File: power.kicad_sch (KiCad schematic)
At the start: 12 parts, among them J301 USB_C_Receptacle_USB2.0, U301 FTZU6.2ET148, U302 XC9265A331MR-G

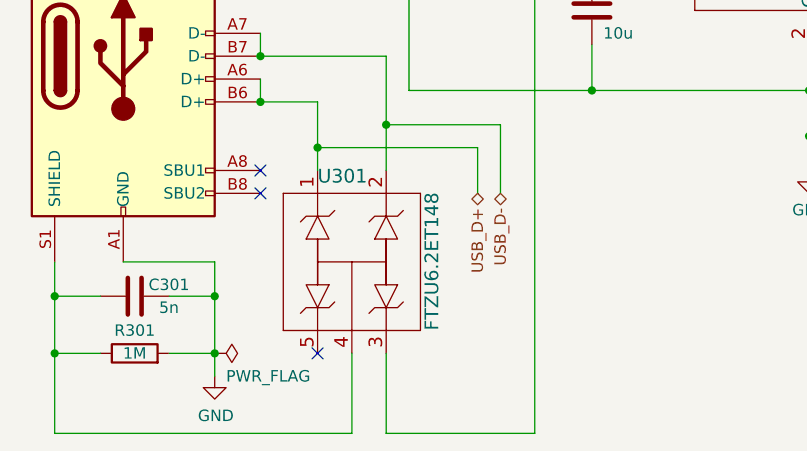
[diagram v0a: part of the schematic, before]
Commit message: replace out of stock components
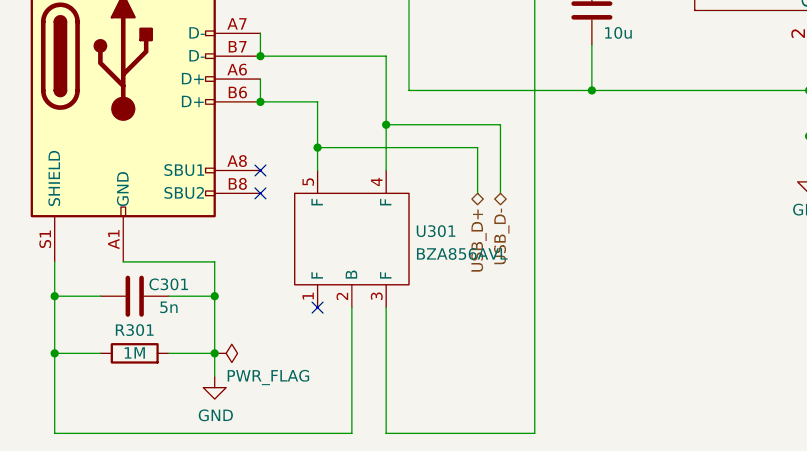
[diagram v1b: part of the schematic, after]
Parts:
- removed U301: FTZU6.2ET148, FTZU6.2ET148:FTZU6.2ET148, symbol FTZU6.2ET148:FTZU6.2ET148
- added U301: BZA856AVL, BZA856AVL:BZA856AVL, symbol BZA956A:BZA956A
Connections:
- net +5V: now also U301.3 (F)
- net USB_D+: now also U301.5 (F)
- net USB_D-: now also U301.4 (F)
- net at C301.1, J301.S1 (SHIELD), R301.1: now also U301.2 (B)
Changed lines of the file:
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@@
   (junction (at 63.5 107.95) (diameter 0) (color 0 0 0 0)
   )
-  (no_connect (at 92.71 114.3))
+  (no_connect (at 92.71 109.22))
   (no_connect (at 86.36 93.98))
   (no_connect (at 86.36 96.52))
@@
     (stroke (width 0) (type default) (color 0 0 0 0))
   )
+  (wire (pts (xy 100.33 109.22) (xy 100.33 123.19))
+    (stroke (width 0) (type default) (color 0 0 0 0))
+  )
   (wire (pts (xy 68.58 114.3) (xy 63.5 114.3))
     (stroke (width 0) (type default) (color 0 0 0 0))
@@
     (stroke (width 0) (type default) (color 0 0 0 0))
   )
-  (wire (pts (xy 96.52 114.3) (xy 96.52 123.19))
-    (stroke (width 0) (type default) (color 0 0 0 0))
-  )
-  (wire (pts (xy 100.33 114.3) (xy 100.33 123.19))
+  (wire (pts (xy 96.52 109.22) (xy 96.52 123.19))
     (stroke (width 0) (type default) (color 0 0 0 0))
   )
@@
   (symbol (lib_id "power:PWR_FLAG") (at 81.28 114.3 270) (unit 1)
     (in_bom yes) (on_board yes)
-    (property "Reference" "#FLG0101" (id 0) (at 83.185 114.3 0)
+    (property "Reference" "#FLG0301" (id 0) (at 83.185 114.3 0)
       (effects (font (size 1.27 1.27)) hide)
     )
@@
   (symbol (lib_id "power:+3V3") (at 181.61 63.5 0) (unit 1)
     (in_bom yes) (on_board yes)
-    (property "Reference" "#PWR0303" (id 0) (at 181.61 67.31 0)
+    (property "Reference" "#PWR0304" (id 0) (at 181.61 67.31 0)
       (effects (font (size 1.27 1.27)) hide)
     )
@@
     (pin "2")
   )
+  (symbol (lib_id "BZA956A:BZA956A") (at 96.52 101.6 0) (unit 1)
+    (in_bom yes) (on_board yes)
+    (property "Reference" "U301" (id 0) (at 103.5812 100.7653 0)
+      (effects (font (size 1.27 1.27)) (justify left))
+    )
+    (property "Value" "BZA856AVL" (id 1) (at 103.5812 103.3022 0)
+      (effects (font (size 1.27 1.27)) (justify left))
+    )
+    (property "Footprint" "BZA856AVL:BZA856AVL" (id 2) (at 96.52 101.6 0)
+      (effects (font (size 1.27 1.27)) hide)
+    )
+    (property "Datasheet" "https://assets.nexperia.com/documents/data-sheet/BZA800AVL_SERIES.pdf" (id 3) (at 96.52 101.6 0)
+      (effects (font (size 1.27 1.27)) hide)
+    )
+    (property "DK" "https://www.digikey.no/no/products/detail/nexperia-usa-inc/BZA856AVL-115/1155404" (id 4) (at 96.52 101.6 0)
+      (effects (font (size 1.27 1.27)) hide)
+    )
+    (pin "1")
+    (pin "2")
+    (pin "3")
+    (pin "4")
+    (pin "5")
+  )
   (symbol (lib_id "Device:R") (at 72.39 114.3 90) (unit 1)
     (in_bom yes) (on_board yes)
@@
     (pin "2")
   )
-  (symbol (lib_id "FTZU6.2ET148:FTZU6.2ET148") (at 96.52 104.14 0) (unit 1)
-    (in_bom yes) (on_board yes)
-    (property "Reference" "U301" (id 0) (at 92.71 94.615 0)
-      (effects (font (size 1.524 1.524)) (justify left))
-    )
-    (property "Value" "FTZU6.2ET148" (id 1) (at 105.41 111.76 90)
-      (effects (font (size 1.524 1.524)) (justify left))
-    )
-    (property "Footprint" "FTZU6.2ET148:FTZU6.2ET148" (id 2) (at 116.205 106.68 0)
-      (effects (font (size 1.524 1.524)) hide)
-    )
-    (property "Datasheet" "" (id 3) (at 96.52 104.14 0)
-      (effects (font (size 1.524 1.524)))
-    )
-    (property "DK" "https://www.digikey.no/no/products/detail/rohm-semiconductor/FTZU6-2ET148/926206" (id 4) (at 96.52 104.14 0)
-      (effects (font (size 1.27 1.27)) hide)
-    )
-    (pin "1")
-    (pin "2")
-    (pin "3")
-    (pin "4")
-    (pin "5")
-  )
   (symbol (lib_id "power:+5V") (at 102.87 63.5 0) (unit 1)
     (in_bom yes) (on_board yes) (fields_autoplaced)
-    (property "Reference" "#PWR0115" (id 0) (at 102.87 67.31 0)
+    (property "Reference" "#PWR0302" (id 0) (at 102.87 67.31 0)
       (effects (font (size 1.27 1.27)) hide)
     )
@@
   (symbol (lib_id "power:GND") (at 147.32 93.98 0) (unit 1)
     (in_bom yes) (on_board yes)
-    (property "Reference" "#PWR0302" (id 0) (at 147.32 100.33 0)
+    (property "Reference" "#PWR0303" (id 0) (at 147.32 100.33 0)
       (effects (font (size 1.27 1.27)) hide)
     )
@@
   (symbol (lib_id "power:PWR_FLAG") (at 93.98 63.5 0) (unit 1)
     (in_bom yes) (on_board yes) (fields_autoplaced)
-    (property "Reference" "#FLG0103" (id 0) (at 93.98 61.595 0)
-      (effects (font (size 1.27 1.27)) hide)
-    )
+    (property "Reference" "#FLG0302" (id 0) (at 93.98 61.595 0)
+      (effects (font (size 1.27 1.27)) hide)
+    )

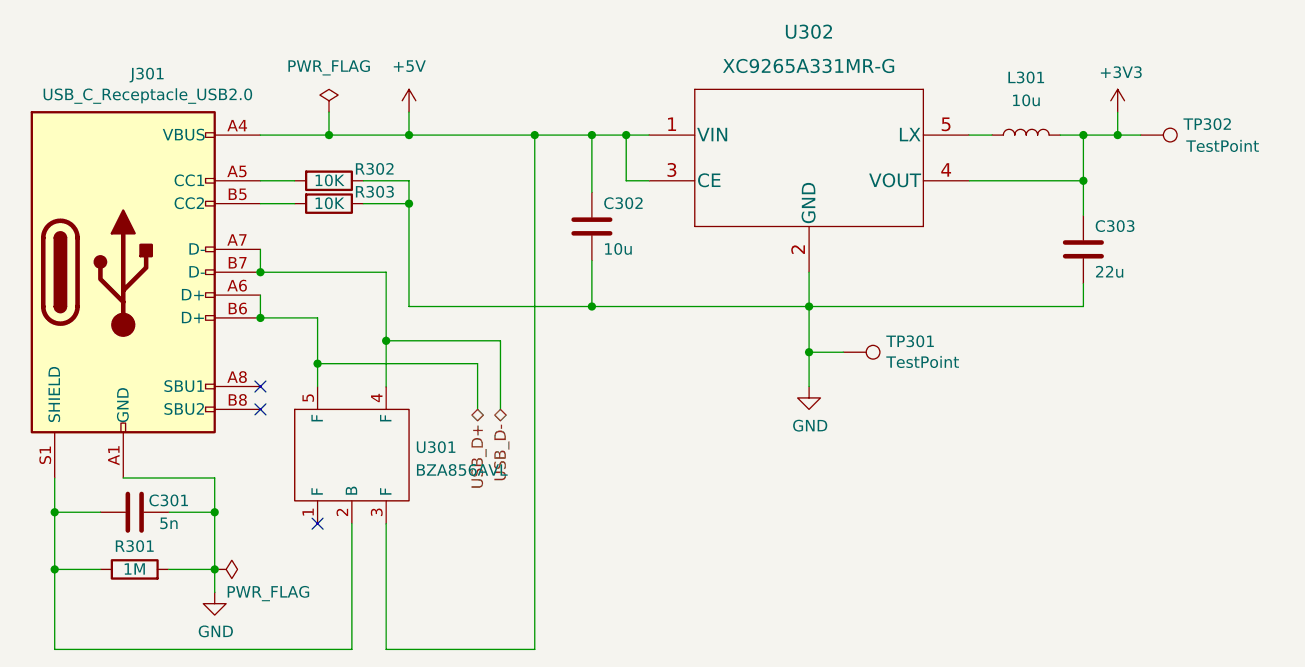
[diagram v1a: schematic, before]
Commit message: reroute new components
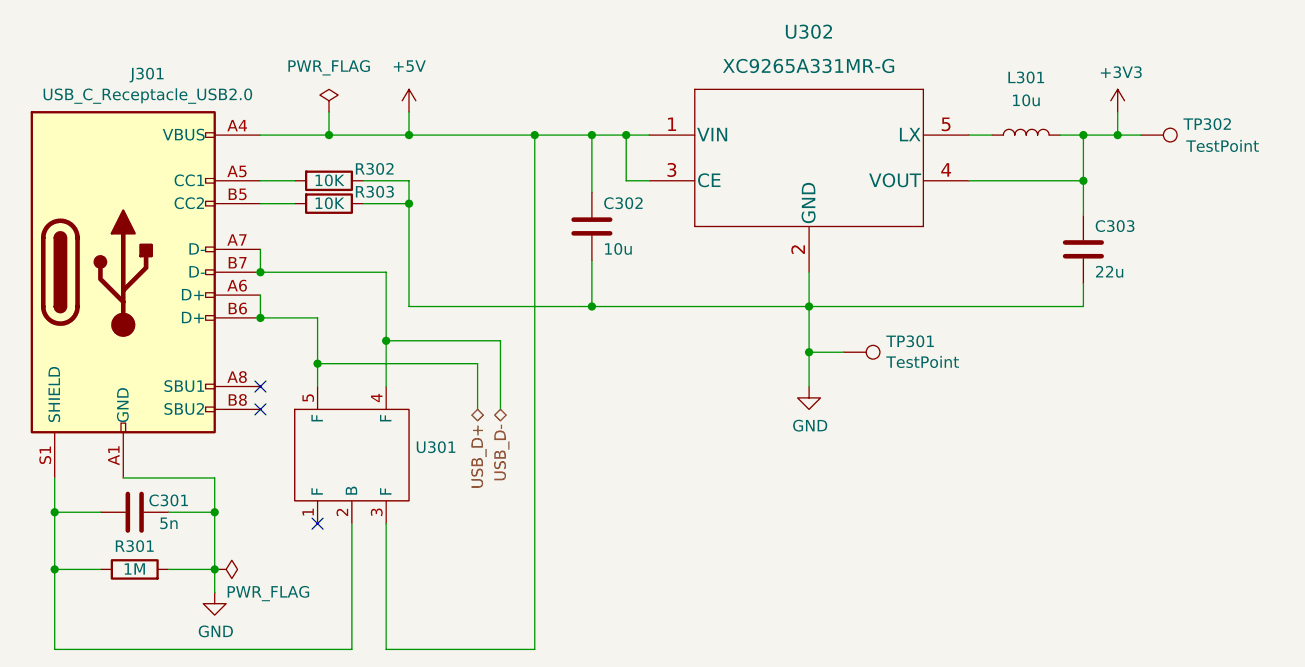
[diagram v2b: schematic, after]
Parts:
- U301: value BZA856AVL -> (none); footprint BZA856AVL:BZA856AVL -> (none)
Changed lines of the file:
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@@
   (junction (at 147.32 90.17) (diameter 0) (color 0 0 0 0)
   )
+  (junction (at 100.33 88.9) (diameter 0) (color 0 0 0 0)
+  )
   (junction (at 123.19 85.09) (diameter 0) (color 0 0 0 0)
   )
   (junction (at 63.5 114.3) (diameter 0) (color 0 0 0 0)
   )
+  (junction (at 86.36 86.36) (diameter 0) (color 0 0 0 0)
+  )
+  (junction (at 147.32 85.09) (diameter 0) (color 0 0 0 0)
+  )
   (junction (at 92.71 91.44) (diameter 0) (color 0 0 0 0)
   )
-  (junction (at 86.36 86.36) (diameter 0) (color 0 0 0 0)
-  )
-  (junction (at 147.32 85.09) (diameter 0) (color 0 0 0 0)
-  )
   (junction (at 93.98 66.04) (diameter 0) (color 0 0 0 0)
   )
   (junction (at 81.28 114.3) (diameter 0) (color 0 0 0 0)
-  )
-  (junction (at 100.33 88.9) (diameter 0) (color 0 0 0 0)
   )
   (junction (at 102.87 66.04) (diameter 0) (color 0 0 0 0)
@@
     (stroke (width 0) (type default) (color 0 0 0 0))
   )
-  (wire (pts (xy 110.49 91.44) (xy 92.71 91.44))
+  (wire (pts (xy 100.33 88.9) (xy 113.03 88.9))
     (stroke (width 0) (type default) (color 0 0 0 0))
   )
@@
     (stroke (width 0) (type default) (color 0 0 0 0))
   )
-  (wire (pts (xy 100.33 88.9) (xy 113.03 88.9))
+  (wire (pts (xy 100.33 81.28) (xy 100.33 88.9))
     (stroke (width 0) (type default) (color 0 0 0 0))
   )
@@
     (stroke (width 0) (type default) (color 0 0 0 0))
   )
+  (wire (pts (xy 100.33 88.9) (xy 100.33 93.98))
+    (stroke (width 0) (type default) (color 0 0 0 0))
+  )
   (wire (pts (xy 81.28 107.95) (xy 81.28 104.14))
     (stroke (width 0) (type default) (color 0 0 0 0))
   )
-  (wire (pts (xy 100.33 81.28) (xy 100.33 88.9))
-    (stroke (width 0) (type default) (color 0 0 0 0))
-  )
   (wire (pts (xy 116.84 123.19) (xy 116.84 66.04))
     (stroke (width 0) (type default) (color 0 0 0 0))
   )
+  (wire (pts (xy 90.17 71.12) (xy 86.36 71.12))
+    (stroke (width 0) (type default) (color 0 0 0 0))
+  )
+  (wire (pts (xy 110.49 96.52) (xy 110.49 91.44))
+    (stroke (width 0) (type default) (color 0 0 0 0))
+  )
+  (wire (pts (xy 81.28 114.3) (xy 81.28 116.84))
+    (stroke (width 0) (type default) (color 0 0 0 0))
+  )
+  (wire (pts (xy 86.36 83.82) (xy 86.36 86.36))
+    (stroke (width 0) (type default) (color 0 0 0 0))
+  )
+  (wire (pts (xy 68.58 107.95) (xy 63.5 107.95))
+    (stroke (width 0) (type default) (color 0 0 0 0))
+  )
+  (wire (pts (xy 86.36 78.74) (xy 86.36 81.28))
+    (stroke (width 0) (type default) (color 0 0 0 0))
+  )
+  (wire (pts (xy 177.8 82.55) (xy 177.8 85.09))
+    (stroke (width 0) (type default) (color 0 0 0 0))
+  )
+  (wire (pts (xy 81.28 104.14) (xy 71.12 104.14))
+    (stroke (width 0) (type default) (color 0 0 0 0))
+  )
+  (wire (pts (xy 102.87 71.12) (xy 97.79 71.12))
+    (stroke (width 0) (type default) (color 0 0 0 0))
+  )
+  (wire (pts (xy 165.1 71.12) (xy 177.8 71.12))
+    (stroke (width 0) (type default) (color 0 0 0 0))
+  )
+  (wire (pts (xy 123.19 85.09) (xy 147.32 85.09))
+    (stroke (width 0) (type default) (color 0 0 0 0))
+  )
+  (wire (pts (xy 102.87 73.66) (xy 102.87 71.12))
+    (stroke (width 0) (type default) (color 0 0 0 0))
+  )
+  (wire (pts (xy 123.19 66.04) (xy 127 66.04))
+    (stroke (width 0) (type default) (color 0 0 0 0))
+  )
+  (wire (pts (xy 102.87 63.5) (xy 102.87 66.04))
+    (stroke (width 0) (type default) (color 0 0 0 0))
+  )
   (wire (pts (xy 92.71 91.44) (xy 92.71 93.98))
     (stroke (width 0) (type default) (color 0 0 0 0))
   )
-  (wire (pts (xy 90.17 71.12) (xy 86.36 71.12))
-    (stroke (width 0) (type default) (color 0 0 0 0))
-  )
-  (wire (pts (xy 110.49 96.52) (xy 110.49 91.44))
-    (stroke (width 0) (type default) (color 0 0 0 0))
-  )
-  (wire (pts (xy 81.28 114.3) (xy 81.28 116.84))
-    (stroke (width 0) (type default) (color 0 0 0 0))
-  )
-  (wire (pts (xy 86.36 83.82) (xy 86.36 86.36))
-    (stroke (width 0) (type default) (color 0 0 0 0))
-  )
-  (wire (pts (xy 68.58 107.95) (xy 63.5 107.95))
-    (stroke (width 0) (type default) (color 0 0 0 0))
-  )
-  (wire (pts (xy 86.36 78.74) (xy 86.36 81.28))
-    (stroke (width 0) (type default) (color 0 0 0 0))
-  )
-  (wire (pts (xy 177.8 82.55) (xy 177.8 85.09))
-    (stroke (width 0) (type default) (color 0 0 0 0))
-  )
-  (wire (pts (xy 81.28 104.14) (xy 71.12 104.14))
-    (stroke (width 0) (type default) (color 0 0 0 0))
-  )
-  (wire (pts (xy 102.87 71.12) (xy 97.79 71.12))
-    (stroke (width 0) (type default) (color 0 0 0 0))
-  )
-  (wire (pts (xy 165.1 71.12) (xy 177.8 71.12))
-    (stroke (width 0) (type default) (color 0 0 0 0))
-  )
-  (wire (pts (xy 123.19 85.09) (xy 147.32 85.09))
-    (stroke (width 0) (type default) (color 0 0 0 0))
-  )
-  (wire (pts (xy 100.33 88.9) (xy 100.33 93.98))
-    (stroke (width 0) (type default) (color 0 0 0 0))
-  )
-  (wire (pts (xy 102.87 73.66) (xy 102.87 71.12))
-    (stroke (width 0) (type default) (color 0 0 0 0))
-  )
-  (wire (pts (xy 123.19 66.04) (xy 127 66.04))
-    (stroke (width 0) (type default) (color 0 0 0 0))
-  )
-  (wire (pts (xy 102.87 63.5) (xy 102.87 66.04))
-    (stroke (width 0) (type default) (color 0 0 0 0))
-  )
   (wire (pts (xy 100.33 109.22) (xy 100.33 123.19))
     (stroke (width 0) (type default) (color 0 0 0 0))
@@
   )
   (wire (pts (xy 147.32 93.98) (xy 147.32 90.17))
+    (stroke (width 0) (type default) (color 0 0 0 0))
+  )
+  (wire (pts (xy 92.71 91.44) (xy 110.49 91.44))
     (stroke (width 0) (type default) (color 0 0 0 0))
   )
@@
       (effects (font (size 1.27 1.27)) (justify left))
     )
-    (property "Value" "BZA856AVL" (id 1) (at 103.5812 103.3022 0)
-      (effects (font (size 1.27 1.27)) (justify left))
-    )
-    (property "Footprint" "BZA856AVL:BZA856AVL" (id 2) (at 96.52 101.6 0)
-      (effects (font (size 1.27 1.27)) hide)
-    )
+    (property "Value" "" (id 1) (at 91.44 101.6 0)
+      (effects (font (size 1.27 1.27)) (justify left))
+    )
+    (property "Footprint" "" (id 2) (at 96.52 101.6 0)
+      (effects (font (size 1.27 1.27)) hide)
+    )

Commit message: påske
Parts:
- U301: value (none) -> BZA856AVL; footprint (none) -> BZA856AVL:BZA856AVL
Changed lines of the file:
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@@
       (effects (font (size 1.27 1.27)) (justify left))
     )
-    (property "Value" "" (id 1) (at 91.44 101.6 0)
+    (property "Value" "BZA856AVL" (id 1) (at 91.44 101.6 0)
       (effects (font (size 1.27 1.27)) (justify left))
     )
-    (property "Footprint" "" (id 2) (at 96.52 101.6 0)
+    (property "Footprint" "BZA856AVL:BZA856AVL" (id 2) (at 96.52 101.6 0)
       (effects (font (size 1.27 1.27)) hide)
     )

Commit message: final component changes
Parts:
- C301: value 5n -> (none); footprint Capacitor_SMD:C_0805_2012Metric -> (none)
- C302: value 10u -> (none); footprint Capacitor_SMD:C_0805_2012Metric -> (none)
- C303: value 22u -> (none); footprint Capacitor_SMD:C_0805_2012Metric -> (none)
- J301: value USB_C_Receptacle_USB2.0 -> (none); footprint USB4110-GF-A:USB4110-GF-A -> (none)
- L301: value 10u -> (none); footprint Inductor_SMD:L_0805_2012Metric -> (none)
- R301: value 1M -> (none); footprint Resistor_SMD:R_0805_2012Metric -> (none)
- R302, R303: value 10K -> (none); footprint Resistor_SMD:R_0805_2012Metric -> (none)
- TP301, TP302: value TestPoint -> (none); footprint TestPoint:TestPoint_Pad_D1.5mm -> (none)
- U301: value BZA856AVL -> (none); footprint BZA856AVL:BZA856AVL -> (none)
- U302: value XC9265A331MR-G -> (none); footprint XC9265A331MR-G:XC9265A331MR-G -> (none)
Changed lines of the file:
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@@
     (in_bom yes) (on_board yes)
     (property "Reference" "R303" (id 0) (at 99.06 72.39 90))
-    (property "Value" "10K" (id 1) (at 93.98 73.66 90))
-    (property "Footprint" "Resistor_SMD:R_0805_2012Metric" (id 2) (at 93.98 71.882 90)
+    (property "Value" "" (id 1) (at 93.98 73.66 90))
+    (property "Footprint" "" (id 2) (at 93.98 71.882 90)
       (effects (font (size 1.27 1.27)) hide)
     )
@@
     (in_bom yes) (on_board yes)
     (property "Reference" "R302" (id 0) (at 99.06 69.85 90))
-    (property "Value" "10K" (id 1) (at 93.98 71.12 90))
-    (property "Footprint" "Resistor_SMD:R_0805_2012Metric" (id 2) (at 93.98 69.342 90)
+    (property "Value" "" (id 1) (at 93.98 71.12 90))
+    (property "Footprint" "" (id 2) (at 93.98 69.342 90)
       (effects (font (size 1.27 1.27)) hide)
     )
@@
       (effects (font (size 1.27 1.27)) (justify left))
     )
-    (property "Value" "TestPoint" (id 1) (at 155.9052 91.313 90)
-      (effects (font (size 1.27 1.27)) (justify left))
-    )
-    (property "Footprint" "TestPoint:TestPoint_Pad_D1.5mm" (id 2) (at 151.13 95.25 0)
+    (property "Value" "" (id 1) (at 155.9052 91.313 90)
+      (effects (font (size 1.27 1.27)) (justify left))
+    )
+    (property "Footprint" "" (id 2) (at 151.13 95.25 0)
       (effects (font (size 1.27 1.27)) hide)
     )
@@
     (in_bom yes) (on_board yes) (fields_autoplaced)
     (property "Reference" "L301" (id 0) (at 171.45 59.69 90))
-    (property "Value" "10u" (id 1) (at 171.45 62.23 90))
-    (property "Footprint" "Inductor_SMD:L_0805_2012Metric" (id 2) (at 171.45 66.04 0)
+    (property "Value" "" (id 1) (at 171.45 62.23 90))
+    (property "Footprint" "" (id 2) (at 171.45 66.04 0)
       (effects (font (size 1.27 1.27)) hide)
     )
@@
     (in_bom yes) (on_board yes)
     (property "Reference" "C301" (id 0) (at 76.2 106.68 90))
-    (property "Value" "5n" (id 1) (at 76.2 109.22 90))
-    (property "Footprint" "Capacitor_SMD:C_0805_2012Metric" (id 2) (at 76.2 106.9848 0)
+    (property "Value" "" (id 1) (at 76.2 109.22 90))
+    (property "Footprint" "" (id 2) (at 76.2 106.9848 0)
       (effects (font (size 1.27 1.27)) hide)
     )
@@
       (effects (font (size 1.27 1.27)) (justify left))
     )
-    (property "Value" "BZA856AVL" (id 1) (at 91.44 101.6 0)
-      (effects (font (size 1.27 1.27)) (justify left))
-    )
-    (property "Footprint" "BZA856AVL:BZA856AVL" (id 2) (at 96.52 101.6 0)
+    (property "Value" "" (id 1) (at 91.44 101.6 0)
+      (effects (font (size 1.27 1.27)) (justify left))
+    )
+    (property "Footprint" "" (id 2) (at 96.52 101.6 0)
       (effects (font (size 1.27 1.27)) hide)
     )
@@
     (in_bom yes) (on_board yes)
     (property "Reference" "R301" (id 0) (at 72.39 111.76 90))
-    (property "Value" "1M" (id 1) (at 72.39 114.3 90))
-    (property "Footprint" "Resistor_SMD:R_0805_2012Metric" (id 2) (at 72.39 116.078 90)
+    (property "Value" "" (id 1) (at 72.39 114.3 90))
+    (property "Footprint" "" (id 2) (at 72.39 116.078 90)
       (effects (font (size 1.27 1.27)) hide)
     )
@@
     (in_bom yes) (on_board yes)
     (property "Reference" "J301" (id 0) (at 73.8378 59.2582 0))
-    (property "Value" "USB_C_Receptacle_USB2.0" (id 1) (at 73.8378 61.5696 0))
-    (property "Footprint" "USB4110-GF-A:USB4110-GF-A" (id 2) (at 74.93 81.28 0)
+    (property "Value" "" (id 1) (at 73.8378 61.5696 0))
+    (property "Footprint" "" (id 2) (at 74.93 81.28 0)
       (effects (font (size 1.27 1.27)) hide)
     )
@@
       (effects (font (size 1.27 1.27)) (justify left))
     )
-    (property "Value" "TestPoint" (id 1) (at 189.23 67.31 90)
-      (effects (font (size 1.27 1.27)) (justify left))
-    )
-    (property "Footprint" "TestPoint:TestPoint_Pad_D1.5mm" (id 2) (at 184.15 71.12 0)
+    (property "Value" "" (id 1) (at 189.23 67.31 90)
+      (effects (font (size 1.27 1.27)) (justify left))
+    )
+    (property "Footprint" "" (id 2) (at 184.15 71.12 0)
       (effects (font (size 1.27 1.27)) hide)
     )
@@
       (effects (font (size 1.27 1.27)) (justify left))
     )
-    (property "Value" "22u" (id 1) (at 179.07 81.28 0)
-      (effects (font (size 1.27 1.27)) (justify left))
-    )
-    (property "Footprint" "Capacitor_SMD:C_0805_2012Metric" (id 2) (at 178.7652 82.55 0)
+    (property "Value" "" (id 1) (at 179.07 81.28 0)
+      (effects (font (size 1.27 1.27)) (justify left))
+    )
+    (property "Footprint" "" (id 2) (at 178.7652 82.55 0)
       (effects (font (size 1.27 1.27)) hide)
     )
@@
       (effects (font (size 1.524 1.524)))
     )
-    (property "Value" "XC9265A331MR-G" (id 1) (at 147.32 58.42 0)
+    (property "Value" "" (id 1) (at 147.32 58.42 0)
       (effects (font (size 1.524 1.524)))
     )
-    (property "Footprint" "XC9265A331MR-G:XC9265A331MR-G" (id 2) (at 147.32 59.944 0)
+    (property "Footprint" "" (id 2) (at 147.32 59.944 0)
       (effects (font (size 1.524 1.524)) hide)
     )
@@
       (effects (font (size 1.27 1.27)) (justify left))
     )
-    (property "Value" "10u" (id 1) (at 124.46 78.74 0)
-      (effects (font (size 1.27 1.27)) (justify left))
-    )
-    (property "Footprint" "Capacitor_SMD:C_0805_2012Metric" (id 2) (at 124.1552 80.01 0)
-      (effects (font (size 1.27 1.27)) hide)
-    )
+    (property "Value" "" (id 1) (at 124.46 78.74 0)
+      (effects (font (size 1.27 1.27)) (justify left))
+    )
+    (property "Footprint" "" (id 2) (at 124.1552 80.01 0)
+      (effects (font (size 1.27 1.27)) hide)
+    )
